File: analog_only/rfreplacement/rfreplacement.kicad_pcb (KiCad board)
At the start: 2 copper layers, 16.5 x 52.1 mm, 24 parts

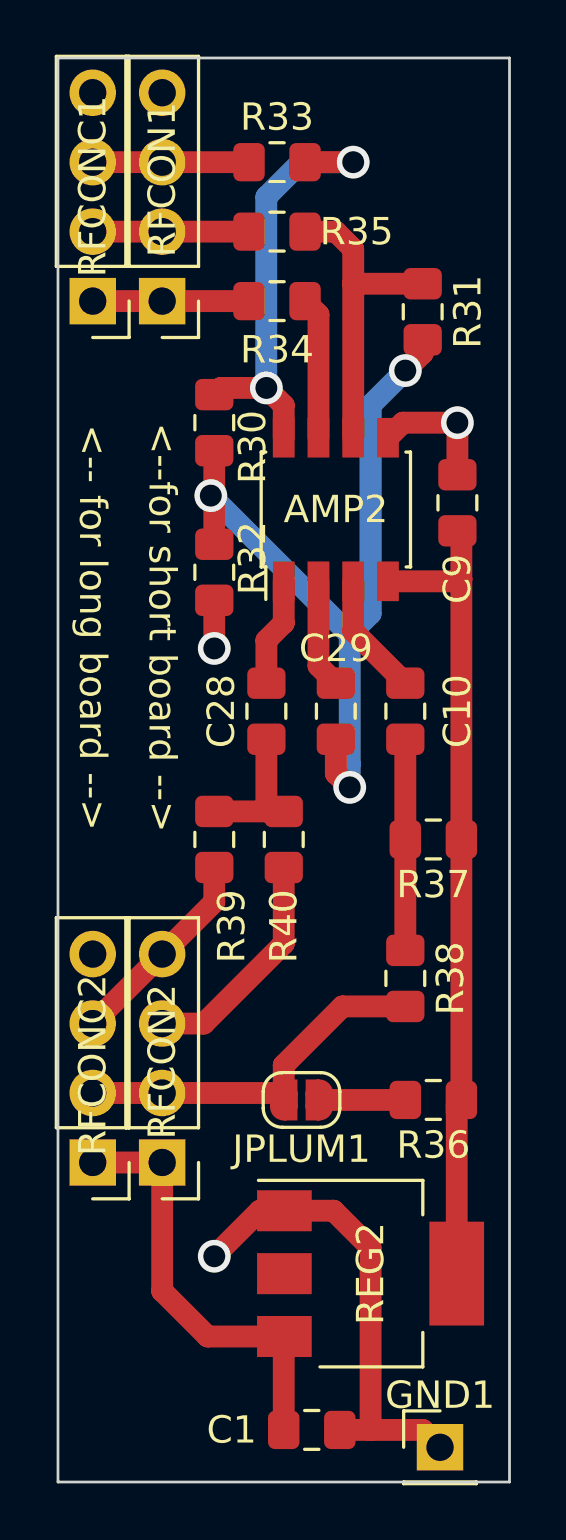
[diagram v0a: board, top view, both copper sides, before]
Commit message: Tidy up layout a bit
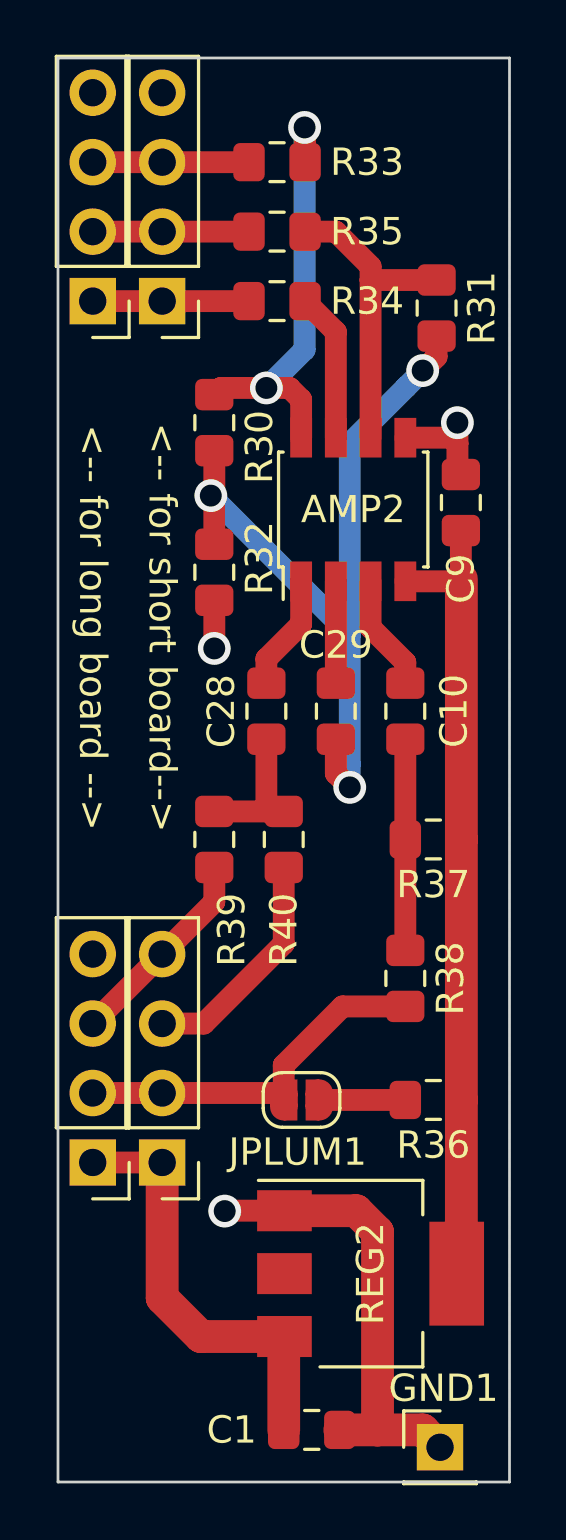
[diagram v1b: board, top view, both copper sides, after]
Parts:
- moved AMP2 0.64 mm to (114.9, 78.7)
- moved R31 0.53 mm to (118.0, 71.4)
- moved C9 0.13 mm to (118.9, 78.5)
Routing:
- net GNDA: track 32.4 -> 31.2 mm
- net /3V3X: track 30.0 -> 29.3 mm
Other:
- board text added: "<-- for short board-->"
- board text removed: "<--for short board -->"
